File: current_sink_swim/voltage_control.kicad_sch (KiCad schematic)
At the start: 7 parts, among them U1 LMV358

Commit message: re-annotate schematic
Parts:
- renumbered R9 to R4
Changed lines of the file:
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@@
         )
         (path "/d8f9bd22-1078-406d-bafe-f69bb2710c23/114b53f6-b762-4b90-a865-8e9ebeba9179"
-          (reference "#PWR07") (unit 1)
+          (reference "#PWR06") (unit 1)
         )
       )
@@
         )
         (path "/d8f9bd22-1078-406d-bafe-f69bb2710c23/114b53f6-b762-4b90-a865-8e9ebeba9179"
-          (reference "R8") (unit 1)
+          (reference "R6") (unit 1)
         )
       )
@@
         )
         (path "/d8f9bd22-1078-406d-bafe-f69bb2710c23/114b53f6-b762-4b90-a865-8e9ebeba9179"
-          (reference "R7") (unit 1)
+          (reference "R5") (unit 1)
         )
       )
@@
         )
         (path "/d8f9bd22-1078-406d-bafe-f69bb2710c23/114b53f6-b762-4b90-a865-8e9ebeba9179"
-          (reference "U3") (unit 2)
+          (reference "U2") (unit 2)
         )
       )
@@
   (symbol (lib_id "Device:R") (at 57.785 141.605 0) (unit 1)
     (in_bom yes) (on_board yes) (dnp no) (fields_autoplaced)
-    (property "Reference" "R9" (at 59.69 140.335 0)
+    (property "Reference" "R4" (at 59.69 140.335 0)
       (effects (font (size 1.27 1.27)) (justify left))
     )
@@
       (project "current_sink_swim"
         (path "/d8f9bd22-1078-406d-bafe-f69bb2710c23/114b53f6-b762-4b90-a865-8e9ebeba9179"
-          (reference "R9") (unit 1)
+          (reference "R4") (unit 1)
         )
       )
@@
         )
         (path "/d8f9bd22-1078-406d-bafe-f69bb2710c23/114b53f6-b762-4b90-a865-8e9ebeba9179"
-          (reference "#PWR08") (unit 1)
+          (reference "#PWR07") (unit 1)
         )
       )
@@
         )
         (path "/d8f9bd22-1078-406d-bafe-f69bb2710c23/114b53f6-b762-4b90-a865-8e9ebeba9179"
-          (reference "U3") (unit 3)
+          (reference "U2") (unit 3)
         )
       )
@@
         )
         (path "/d8f9bd22-1078-406d-bafe-f69bb2710c23/114b53f6-b762-4b90-a865-8e9ebeba9179"
-          (reference "C4") (unit 1)
-        )
-      )
+          (reference "C2") (unit 1)
+        )
+      )

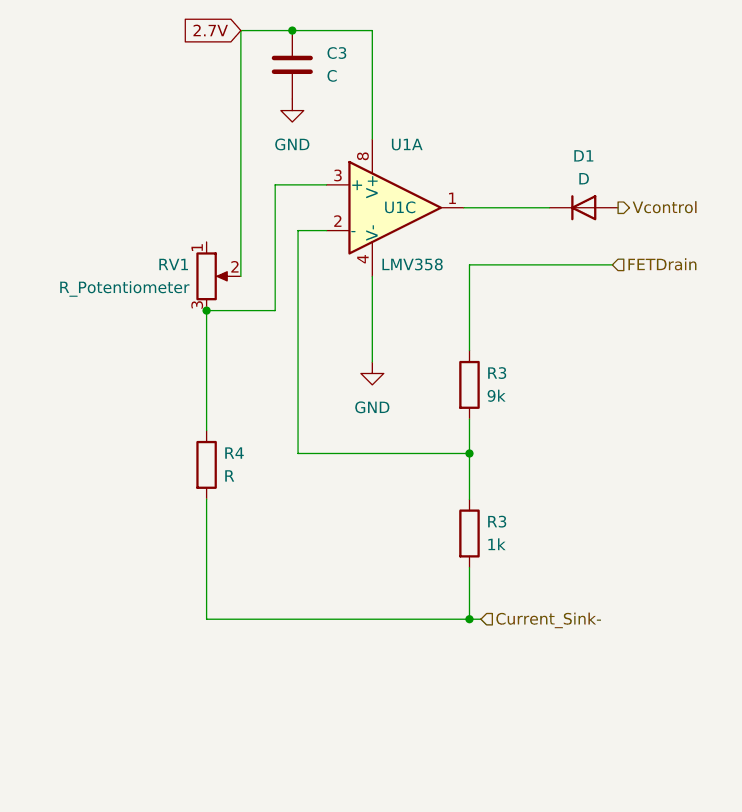
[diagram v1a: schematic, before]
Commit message: assign footprints and start layout
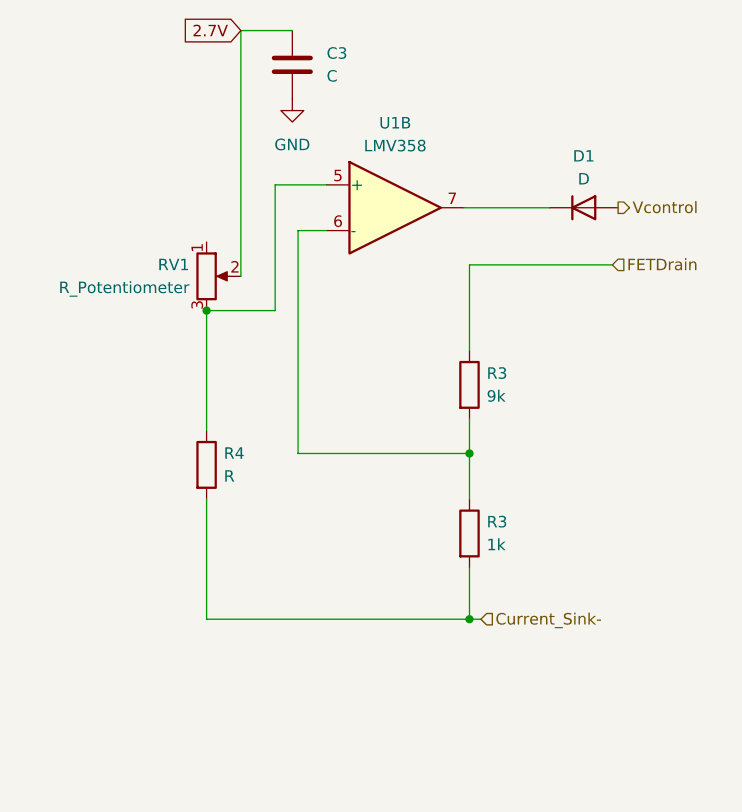
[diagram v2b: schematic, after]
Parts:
- removed U1: LMV358, symbol Amplifier_Operational:LMV358
- added U1: LMV358, Package_SO:SOIC-8_3.9x4.9mm_P1.27mm, symbol Amplifier_Operational:LMV358
- C3: footprint (none) -> Capacitor_SMD:C_0805_2012Metric_Pad1.18x1.45mm_HandSolder
- D1: footprint (none) -> Diode_SMD:D_SOD-323_HandSoldering; MPN (none) -> 1N4148WT-7
- R3, R4: footprint (none) -> Resistor_SMD:R_0805_2012Metric_Pad1.20x1.40mm_HandSolder
- RV1: footprint (none) -> Package_TO_SOT_THT:TO-220-3_Vertical
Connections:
- net at R3.1, R3.2: now also U1.6 (-)
- net at D1.1 (K): now also U1.7
- net at R4.1, RV1.3: now also U1.5 (+)
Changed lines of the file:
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@@
   (junction (at 86.995 140.335) (diameter 0) (color 0 0 0 0)
   )
-  (junction (at 67.31 93.345) (diameter 0) (color 0 0 0 0)
-  )
   (junction (at 57.785 124.46) (diameter 0) (color 0 0 0 0)
   )
@@
     (stroke (width 0) (type default))
   )
-  (wire (pts (xy 76.2 120.65) (xy 76.2 130.175))
-    (stroke (width 0) (type default))
-  )
   (wire (pts (xy 86.36 113.03) (xy 95.885 113.03))
     (stroke (width 0) (type default))
@@
     (stroke (width 0) (type default))
   )
-  (wire (pts (xy 67.31 93.345) (xy 76.2 93.345))
-    (stroke (width 0) (type default))
-  )
   (wire (pts (xy 71.12 115.57) (xy 67.945 115.57))
-    (stroke (width 0) (type default))
-  )
-  (wire (pts (xy 76.2 93.345) (xy 76.2 105.41))
     (stroke (width 0) (type default))
   )
@@
       (effects (font (size 1.27 1.27)) (justify left))
     )
-    (property "Footprint" "" (at 85.217 149.225 90)
+    (property "Footprint" "Resistor_SMD:R_0805_2012Metric_Pad1.20x1.40mm_HandSolder" (at 85.217 149.225 90)
       (effects (font (size 1.27 1.27)) hide)
     )
@@
       (effects (font (size 1.27 1.27)) (justify left))
     )
-    (property "Footprint" "" (at 85.217 132.715 90)
+    (property "Footprint" "Resistor_SMD:R_0805_2012Metric_Pad1.20x1.40mm_HandSolder" (at 85.217 132.715 90)
       (effects (font (size 1.27 1.27)) hide)
     )
@@
     )
   )
-  (symbol (lib_id "Amplifier_Operational:LMV358") (at 78.74 113.03 0) (unit 1)
-    (in_bom yes) (on_board yes) (dnp no)
-    (property "Reference" "U1" (at 80.01 106.045 0)
-      (effects (font (size 1.27 1.27)))
-    )
-    (property "Value" "LMV358" (at 80.645 119.38 0)
-      (effects (font (size 1.27 1.27)))
-    )
-    (property "Footprint" "" (at 78.74 113.03 0)
-      (effects (font (size 1.27 1.27)) hide)
-    )
-    (property "Datasheet" "http://www.ti.com/lit/ds/symlink/lmv324.pdf" (at 78.74 113.03 0)
-      (effects (font (size 1.27 1.27)) hide)
-    )
-    (property "MPN" "" (at 78.74 113.03 0)
+  (symbol (lib_id "Device:R") (at 57.785 141.605 0) (unit 1)
+    (in_bom yes) (on_board yes) (dnp no) (fields_autoplaced)
+    (property "Reference" "R4" (at 59.69 140.335 0)
+      (effects (font (size 1.27 1.27)) (justify left))
+    )
+    (property "Value" "R" (at 59.69 142.875 0)
+      (effects (font (size 1.27 1.27)) (justify left))
+    )
+    (property "Footprint" "Resistor_SMD:R_0805_2012Metric_Pad1.20x1.40mm_HandSolder" (at 56.007 141.605 90)
+      (effects (font (size 1.27 1.27)) hide)
+    )
+    (property "Datasheet" "~" (at 57.785 141.605 0)
+      (effects (font (size 1.27 1.27)) hide)
+    )
+    (pin "1")
+    (pin "2")
+    (instances
+      (project "current_sink_swim"
+        (path "/d8f9bd22-1078-406d-bafe-f69bb2710c23/114b53f6-b762-4b90-a865-8e9ebeba9179"
+          (reference "R4") (unit 1)
+        )
+      )
+    )
+  )
+  (symbol (lib_id "Amplifier_Operational:LMV358") (at 78.74 113.03 0) (unit 2)
+    (in_bom yes) (on_board yes) (dnp no) (fields_autoplaced)
+    (property "Reference" "U1" (at 78.74 103.632 0)
+      (effects (font (size 1.27 1.27)))
+    )
+    (property "Value" "LMV358" (at 78.74 106.172 0)
+      (effects (font (size 1.27 1.27)))
+    )
+    (property "Footprint" "Package_SO:SOIC-8_3.9x4.9mm_P1.27mm" (at 78.74 113.03 0)
+      (effects (font (size 1.27 1.27)) hide)
+    )
+    (property "Datasheet" "https://www.st.com/content/ccc/resource/technical/document/datasheet/b9/d8/3b/8f/a1/8f/46/01/CD00079372.pdf/files/CD00079372.pdf/jcr:content/translations/en.CD00079372.pdf" (at 78.74 113.03 0)
+      (effects (font (size 1.27 1.27)) hide)
+    )
+    (property "MPN" "LMV358IDT" (at 78.74 113.03 0)
       (effects (font (size 1.27 1.27)) hide)
     )
@@
     (instances
       (project "current_sink_swim"
-        (path "/d8f9bd22-1078-406d-bafe-f69bb2710c23"
-          (reference "U1") (unit 1)
-        )
-        (path "/d8f9bd22-1078-406d-bafe-f69bb2710c23/7bb47634-abd5-40f7-90e5-fb54860f3e74"
-          (reference "U1") (unit 1)
-        )
-        (path "/d8f9bd22-1078-406d-bafe-f69bb2710c23/114b53f6-b762-4b90-a865-8e9ebeba9179"
-          (reference "U2") (unit 2)
-        )
-      )
-    )
-  )
-  (symbol (lib_id "Device:R") (at 57.785 141.605 0) (unit 1)
-    (in_bom yes) (on_board yes) (dnp no) (fields_autoplaced)
-    (property "Reference" "R4" (at 59.69 140.335 0)
-      (effects (font (size 1.27 1.27)) (justify left))
-    )
-    (property "Value" "R" (at 59.69 142.875 0)
-      (effects (font (size 1.27 1.27)) (justify left))
-    )
-    (property "Footprint" "" (at 56.007 141.605 90)
-      (effects (font (size 1.27 1.27)) hide)
-    )
-    (property "Datasheet" "~" (at 57.785 141.605 0)
-      (effects (font (size 1.27 1.27)) hide)
-    )
-    (pin "1")
-    (pin "2")
-    (instances
-      (project "current_sink_swim"
-        (path "/d8f9bd22-1078-406d-bafe-f69bb2710c23/114b53f6-b762-4b90-a865-8e9ebeba9179"
-          (reference "R4") (unit 1)
-        )
-      )
-    )
-  )
-  (symbol (lib_id "power:GND") (at 76.2 130.175 0) (unit 1)
-    (in_bom yes) (on_board yes) (dnp no) (fields_autoplaced)
-    (property "Reference" "#PWR02" (at 76.2 136.525 0)
-      (effects (font (size 1.27 1.27)) hide)
-    )
-    (property "Value" "GND" (at 76.2 135.255 0)
-      (effects (font (size 1.27 1.27)))
-    )
-    (property "Footprint" "" (at 76.2 130.175 0)
-      (effects (font (size 1.27 1.27)) hide)
-    )
-    (property "Datasheet" "" (at 76.2 130.175 0)
-      (effects (font (size 1.27 1.27)) hide)
-    )
-    (pin "1")
-    (instances
-      (project "current_sink_swim"
-        (path "/d8f9bd22-1078-406d-bafe-f69bb2710c23"
-          (reference "#PWR02") (unit 1)
-        )
-        (path "/d8f9bd22-1078-406d-bafe-f69bb2710c23/7bb47634-abd5-40f7-90e5-fb54860f3e74"
-          (reference "#PWR02") (unit 1)
-        )
-        (path "/d8f9bd22-1078-406d-bafe-f69bb2710c23/114b53f6-b762-4b90-a865-8e9ebeba9179"
-          (reference "#PWR07") (unit 1)
+        (path "/d8f9bd22-1078-406d-bafe-f69bb2710c23/7bb47634-abd5-40f7-90e5-fb54860f3e74"
+          (reference "U1") (unit 2)
+        )
+        (path "/d8f9bd22-1078-406d-bafe-f69bb2710c23/114b53f6-b762-4b90-a865-8e9ebeba9179"
+          (reference "U1") (unit 2)
         )
       )
@@
       (effects (font (size 1.27 1.27)))
     )
-    (property "Footprint" "" (at 99.695 113.03 0)
-      (effects (font (size 1.27 1.27)) hide)
-    )
-    (property "Datasheet" "~" (at 99.695 113.03 0)
+    (property "Footprint" "Diode_SMD:D_SOD-323_HandSoldering" (at 99.695 113.03 0)
+      (effects (font (size 1.27 1.27)) hide)
+    )
+    (property "Datasheet" "https://www.diodes.com/assets/Datasheets/1N4148WT.pdf" (at 99.695 113.03 0)
       (effects (font (size 1.27 1.27)) hide)
     )
@@
     )
     (property "Sim.Pins" "1=K 2=A" (at 99.695 113.03 0)
+      (effects (font (size 1.27 1.27)) hide)
+    )
+    (property "MPN" "1N4148WT-7" (at 99.695 113.03 0)
       (effects (font (size 1.27 1.27)) hide)
     )
@@
       (effects (font (size 1.27 1.27)) (justify right))
     )
-    (property "Footprint" "" (at 57.785 120.65 0)
+    (property "Footprint" "Package_TO_SOT_THT:TO-220-3_Vertical" (at 57.785 120.65 0)
       (effects (font (size 1.27 1.27)) hide)
     )
@@
     )
   )
-  (symbol (lib_id "Amplifier_Operational:LMV358") (at 78.74 113.03 0) (unit 3)
-    (in_bom yes) (on_board yes) (dnp no) (fields_autoplaced)
-    (property "Reference" "U1" (at 77.47 113.03 0)
-      (effects (font (size 1.27 1.27)) (justify left))
-    )
-    (property "Value" "LMV358" (at 76.835 114.3 0)
-      (effects (font (size 1.27 1.27)) (justify left) hide)
-    )
-    (property "Footprint" "" (at 78.74 113.03 0)
-      (effects (font (size 1.27 1.27)) hide)
-    )
-    (property "Datasheet" "http://www.ti.com/lit/ds/symlink/lmv324.pdf" (at 78.74 113.03 0)
-      (effects (font (size 1.27 1.27)) hide)
-    )
-    (property "MPN" "" (at 78.74 113.03 0)
-      (effects (font (size 1.27 1.27)) hide)
-    )
-    (pin "1")
-    (pin "2")
-    (pin "3")
-    (pin "5")
-    (pin "6")
-    (pin "7")
-    (pin "4")
-    (pin "8")
-    (instances
-      (project "current_sink_swim"
-        (path "/d8f9bd22-1078-406d-bafe-f69bb2710c23"
-          (reference "U1") (unit 3)
-        )
-        (path "/d8f9bd22-1078-406d-bafe-f69bb2710c23/7bb47634-abd5-40f7-90e5-fb54860f3e74"
-          (reference "U1") (unit 3)
-        )
-        (path "/d8f9bd22-1078-406d-bafe-f69bb2710c23/114b53f6-b762-4b90-a865-8e9ebeba9179"
-          (reference "U2") (unit 3)
-        )
-      )
-    )
-  )
   (symbol (lib_id "Device:C") (at 67.31 97.155 0) (unit 1)
     (in_bom yes) (on_board yes) (dnp no) (fields_autoplaced)
@@
       (effects (font (size 1.27 1.27)) (justify left))
     )
-    (property "Footprint" "" (at 68.2752 100.965 0)
-      (effects (font (size 1.27 1.27)) hide)
-    )
+    (property "Footprint" "Capacitor_SMD:C_0805_2012Metric_Pad1.18x1.45mm_HandSolder" (at 68.2752 100.965 0)
+      (effects (font (size 1.27 1.27)) hide)
+    )

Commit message: add correct pot symbols
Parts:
- RV1: footprint Package_TO_SOT_THT:TO-220-3_Vertical -> Potentiometer_THT:Potentiometer_Bourns_PTV09A-2_Single_Horizontal
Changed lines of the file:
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@@
       (effects (font (size 1.27 1.27)) (justify right))
     )
-    (property "Footprint" "Package_TO_SOT_THT:TO-220-3_Vertical" (at 57.785 120.65 0)
+    (property "Footprint" "Potentiometer_THT:Potentiometer_Bourns_PTV09A-2_Single_Horizontal" (at 57.785 120.65 0)
       (effects (font (size 1.27 1.27)) hide)
     )
@@
       (effects (font (size 1.27 1.27)) hide)
     )
+    (property "MPN" "" (at 57.785 120.65 0)
+      (effects (font (size 1.27 1.27)) hide)
+    )

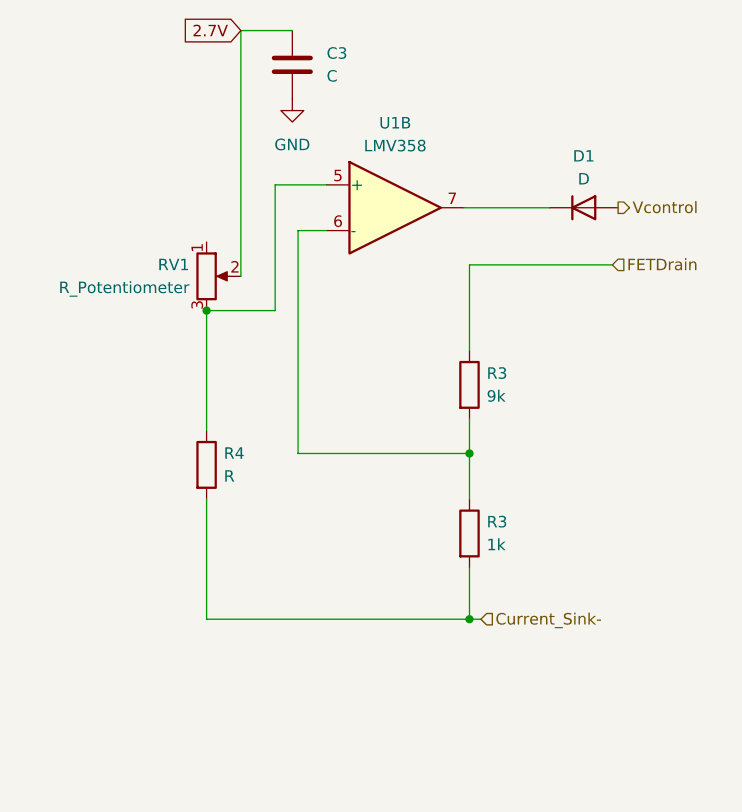
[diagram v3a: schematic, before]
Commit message: clean up potentiometer circuits
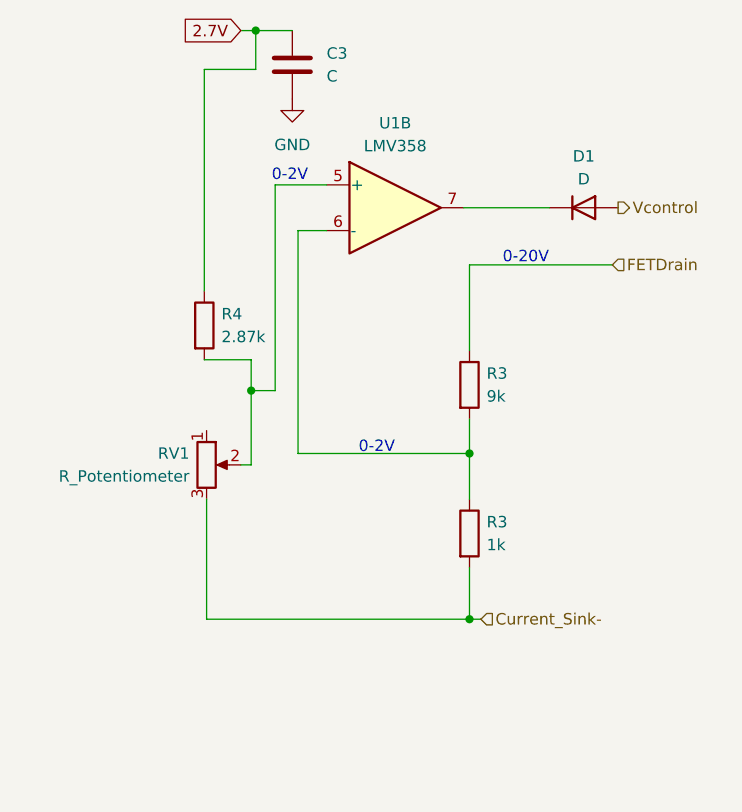
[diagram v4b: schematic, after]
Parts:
- R4: value R -> 2.87k
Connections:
- net 2.7V: now also R4.1; no longer RV1.2
- net Current_Sink-: now also RV1.3; no longer R4.2
- new net: R4.2, RV1.2, U1.5 (+)
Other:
- note added: "0-20V"
- note added: "0-2V"
- moved on the sheet: R4, RV1
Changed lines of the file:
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@@
   (junction (at 86.995 140.335) (diameter 0) (color 0 0 0 0)
   )
-  (junction (at 57.785 124.46) (diameter 0) (color 0 0 0 0)
+  (junction (at 62.738 133.35) (diameter 0) (color 0 0 0 0)
+  )
+  (junction (at 63.246 93.345) (diameter 0) (color 0 0 0 0)
   )
   (junction (at 86.995 158.75) (diameter 0) (color 0 0 0 0)
   )
-  (wire (pts (xy 57.785 124.46) (xy 57.785 137.795))
+  (wire (pts (xy 63.246 93.345) (xy 67.31 93.345))
     (stroke (width 0) (type default))
   )
@@
     (stroke (width 0) (type default))
   )
+  (wire (pts (xy 62.738 129.921) (xy 62.738 133.35))
+    (stroke (width 0) (type default))
+  )
   (wire (pts (xy 86.995 119.38) (xy 102.87 119.38))
     (stroke (width 0) (type default))
   )
-  (wire (pts (xy 57.785 124.46) (xy 65.405 124.46))
+  (wire (pts (xy 57.531 122.301) (xy 57.531 97.663))
     (stroke (width 0) (type default))
   )
@@
     (stroke (width 0) (type default))
   )
-  (wire (pts (xy 65.405 124.46) (xy 65.405 110.49))
+  (wire (pts (xy 63.246 93.345) (xy 63.246 97.663))
+    (stroke (width 0) (type default))
+  )
+  (wire (pts (xy 65.405 110.49) (xy 65.405 133.35))
     (stroke (width 0) (type default))
   )
@@
     (stroke (width 0) (type default))
   )
+  (wire (pts (xy 62.738 141.605) (xy 61.595 141.605))
+    (stroke (width 0) (type default))
+  )
+  (wire (pts (xy 57.531 129.921) (xy 62.738 129.921))
+    (stroke (width 0) (type default))
+  )
   (wire (pts (xy 86.995 128.905) (xy 86.995 119.38))
     (stroke (width 0) (type default))
   )
-  (wire (pts (xy 61.595 93.345) (xy 61.595 120.65))
+  (wire (pts (xy 57.531 97.663) (xy 63.246 97.663))
     (stroke (width 0) (type default))
   )
@@
     (stroke (width 0) (type default))
   )
+  (wire (pts (xy 62.738 133.35) (xy 62.738 141.605))
+    (stroke (width 0) (type default))
+  )
   (wire (pts (xy 57.785 145.415) (xy 57.785 158.75))
     (stroke (width 0) (type default))
@@
     (stroke (width 0) (type default))
   )
-  (wire (pts (xy 61.595 93.345) (xy 67.31 93.345))
+  (wire (pts (xy 61.595 93.345) (xy 63.246 93.345))
     (stroke (width 0) (type default))
   )
@@
   (wire (pts (xy 71.12 115.57) (xy 67.945 115.57))
     (stroke (width 0) (type default))
+  )
+  (wire (pts (xy 65.405 133.35) (xy 62.738 133.35))
+    (stroke (width 0) (type default))
+  )
+  (text "0-2V" (at 65.024 110.236 0)
+    (effects (font (size 1.27 1.27)) (justify left bottom))
+  )
+  (text "0-2V" (at 74.676 140.462 0)
+    (effects (font (size 1.27 1.27)) (justify left bottom))
+  )
+  (text "0-20V" (at 90.678 119.38 0)
+    (effects (font (size 1.27 1.27)) (justify left bottom))
   )
   (global_label "2.7V" (shape input) (at 61.595 93.345 180) (fields_autoplaced)
@@
     )
   )
-  (symbol (lib_id "Device:R") (at 57.785 141.605 0) (unit 1)
-    (in_bom yes) (on_board yes) (dnp no) (fields_autoplaced)
-    (property "Reference" "R4" (at 59.69 140.335 0)
-      (effects (font (size 1.27 1.27)) (justify left))
-    )
-    (property "Value" "R" (at 59.69 142.875 0)
-      (effects (font (size 1.27 1.27)) (justify left))
-    )
-    (property "Footprint" "Resistor_SMD:R_0805_2012Metric_Pad1.20x1.40mm_HandSolder" (at 56.007 141.605 90)
-      (effects (font (size 1.27 1.27)) hide)
-    )
-    (property "Datasheet" "~" (at 57.785 141.605 0)
+  (symbol (lib_id "Device:R") (at 57.531 126.111 0) (unit 1)
+    (in_bom yes) (on_board yes) (dnp no) (fields_autoplaced)
+    (property "Reference" "R4" (at 59.436 124.841 0)
+      (effects (font (size 1.27 1.27)) (justify left))
+    )
+    (property "Value" "2.87k" (at 59.436 127.381 0)
+      (effects (font (size 1.27 1.27)) (justify left))
+    )
+    (property "Footprint" "Resistor_SMD:R_0805_2012Metric_Pad1.20x1.40mm_HandSolder" (at 55.753 126.111 90)
+      (effects (font (size 1.27 1.27)) hide)
+    )
+    (property "Datasheet" "~" (at 57.531 126.111 0)
+      (effects (font (size 1.27 1.27)) hide)
+    )
+    (property "MPN" "" (at 57.531 126.111 0)
       (effects (font (size 1.27 1.27)) hide)
     )
@@
     )
   )
-  (symbol (lib_id "Device:R_Potentiometer") (at 57.785 120.65 0) (unit 1)
-    (in_bom yes) (on_board yes) (dnp no) (fields_autoplaced)
-    (property "Reference" "RV1" (at 55.88 119.38 0)
+  (symbol (lib_id "Device:R_Potentiometer") (at 57.785 141.605 0) (unit 1)
+    (in_bom yes) (on_board yes) (dnp no) (fields_autoplaced)
+    (property "Reference" "RV1" (at 55.88 140.335 0)
       (effects (font (size 1.27 1.27)) (justify right))
     )
-    (property "Value" "R_Potentiometer" (at 55.88 121.92 0)
+    (property "Value" "R_Potentiometer" (at 55.88 142.875 0)
       (effects (font (size 1.27 1.27)) (justify right))
     )
-    (property "Footprint" "Potentiometer_THT:Potentiometer_Bourns_PTV09A-2_Single_Horizontal" (at 57.785 120.65 0)
-      (effects (font (size 1.27 1.27)) hide)
-    )
-    (property "Datasheet" "~" (at 57.785 120.65 0)
-      (effects (font (size 1.27 1.27)) hide)
-    )
-    (property "MPN" "" (at 57.785 120.65 0)
-      (effects (font (size 1.27 1.27)) hide)
-    )
+    (property "Footprint" "Potentiometer_THT:Potentiometer_Bourns_PTV09A-2_Single_Horizontal" (at 57.785 141.605 0)
+      (effects (font (size 1.27 1.27)) hide)
+    )
+    (property "Datasheet" "~" (at 57.785 141.605 0)
+      (effects (font (size 1.27 1.27)) hide)
+    )
+    (property "MPN" "" (at 57.785 141.605 0)
+      (effects (font (size 1.27 1.27)) hide)
+    )
